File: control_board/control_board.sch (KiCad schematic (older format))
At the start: 38 parts, among them J1 Conn_01x08_Male, K1 G5Q-1A, Q1 Q_NPN_BEC, U1 MC78M05_TO252, U2 TSR_1-24120, U3 74LS02, U4 74LS02, U5 Conn_01x08_Male

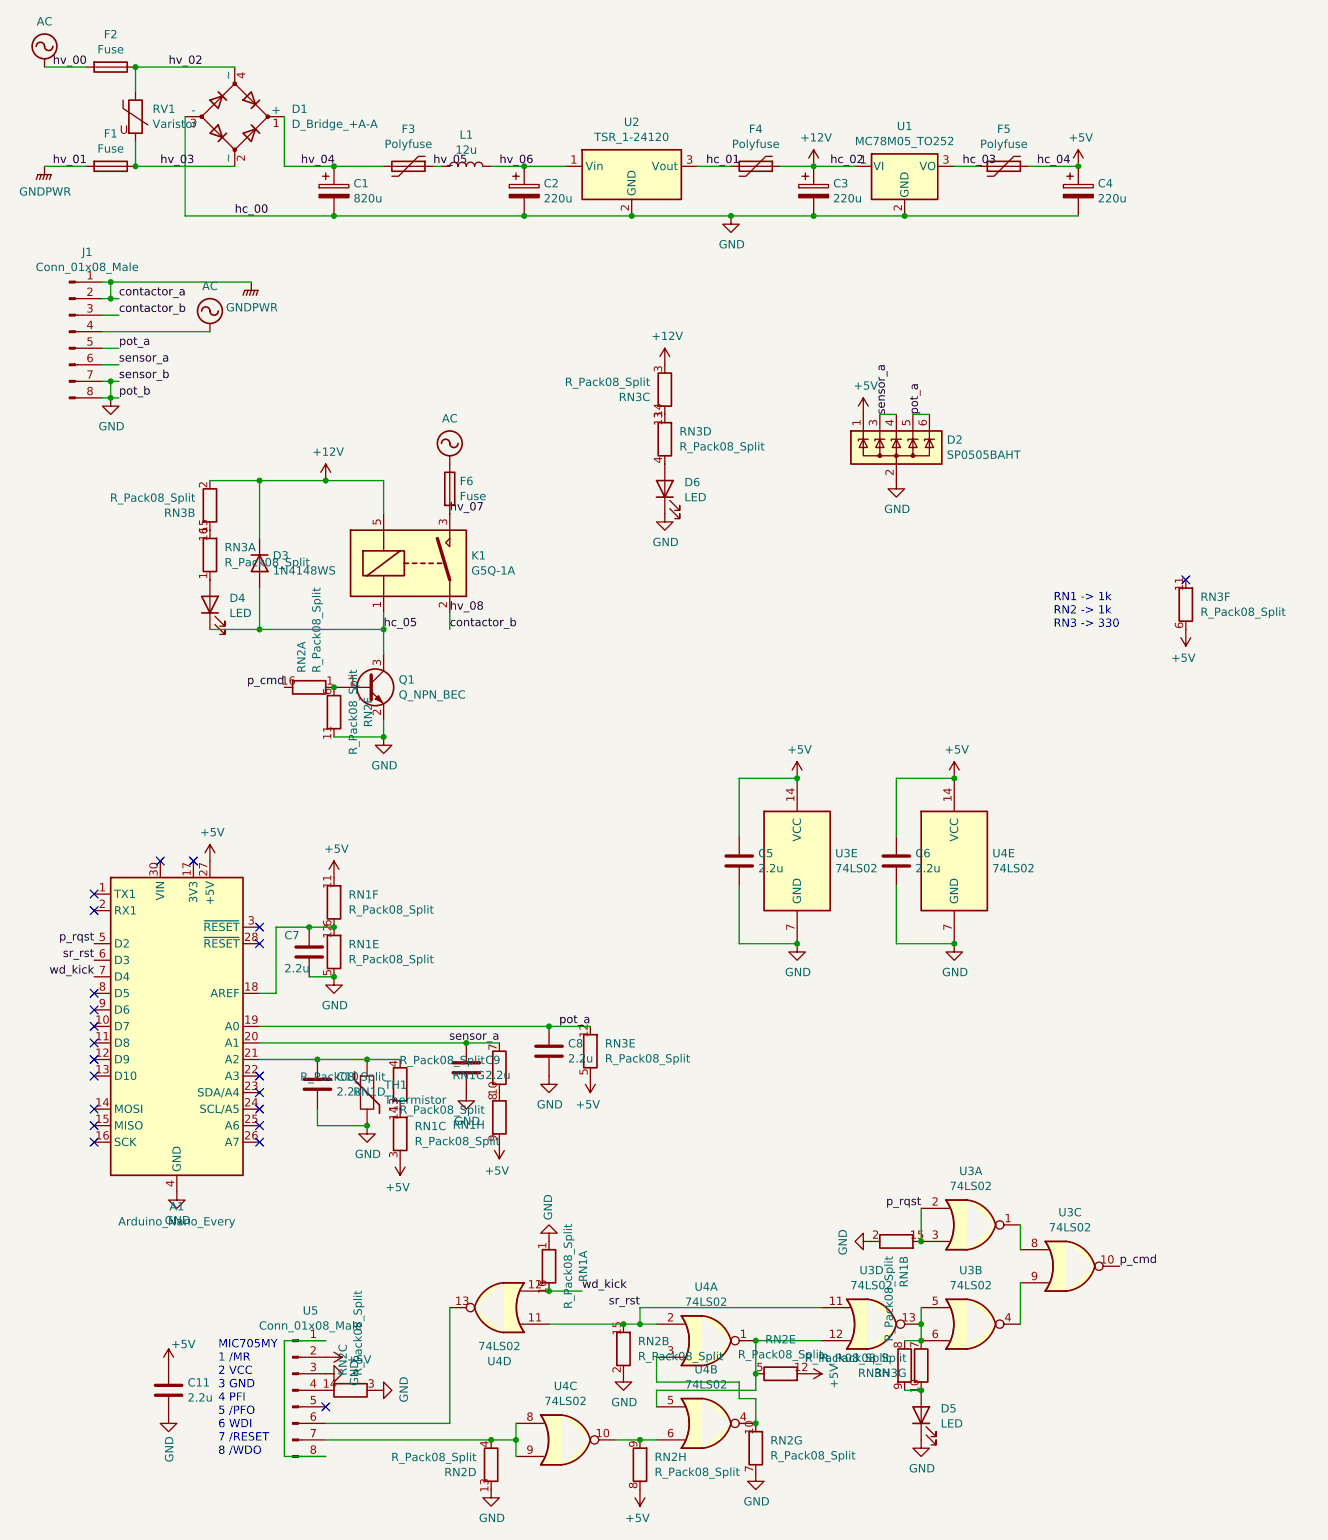
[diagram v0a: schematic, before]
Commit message: Revised PCB layout
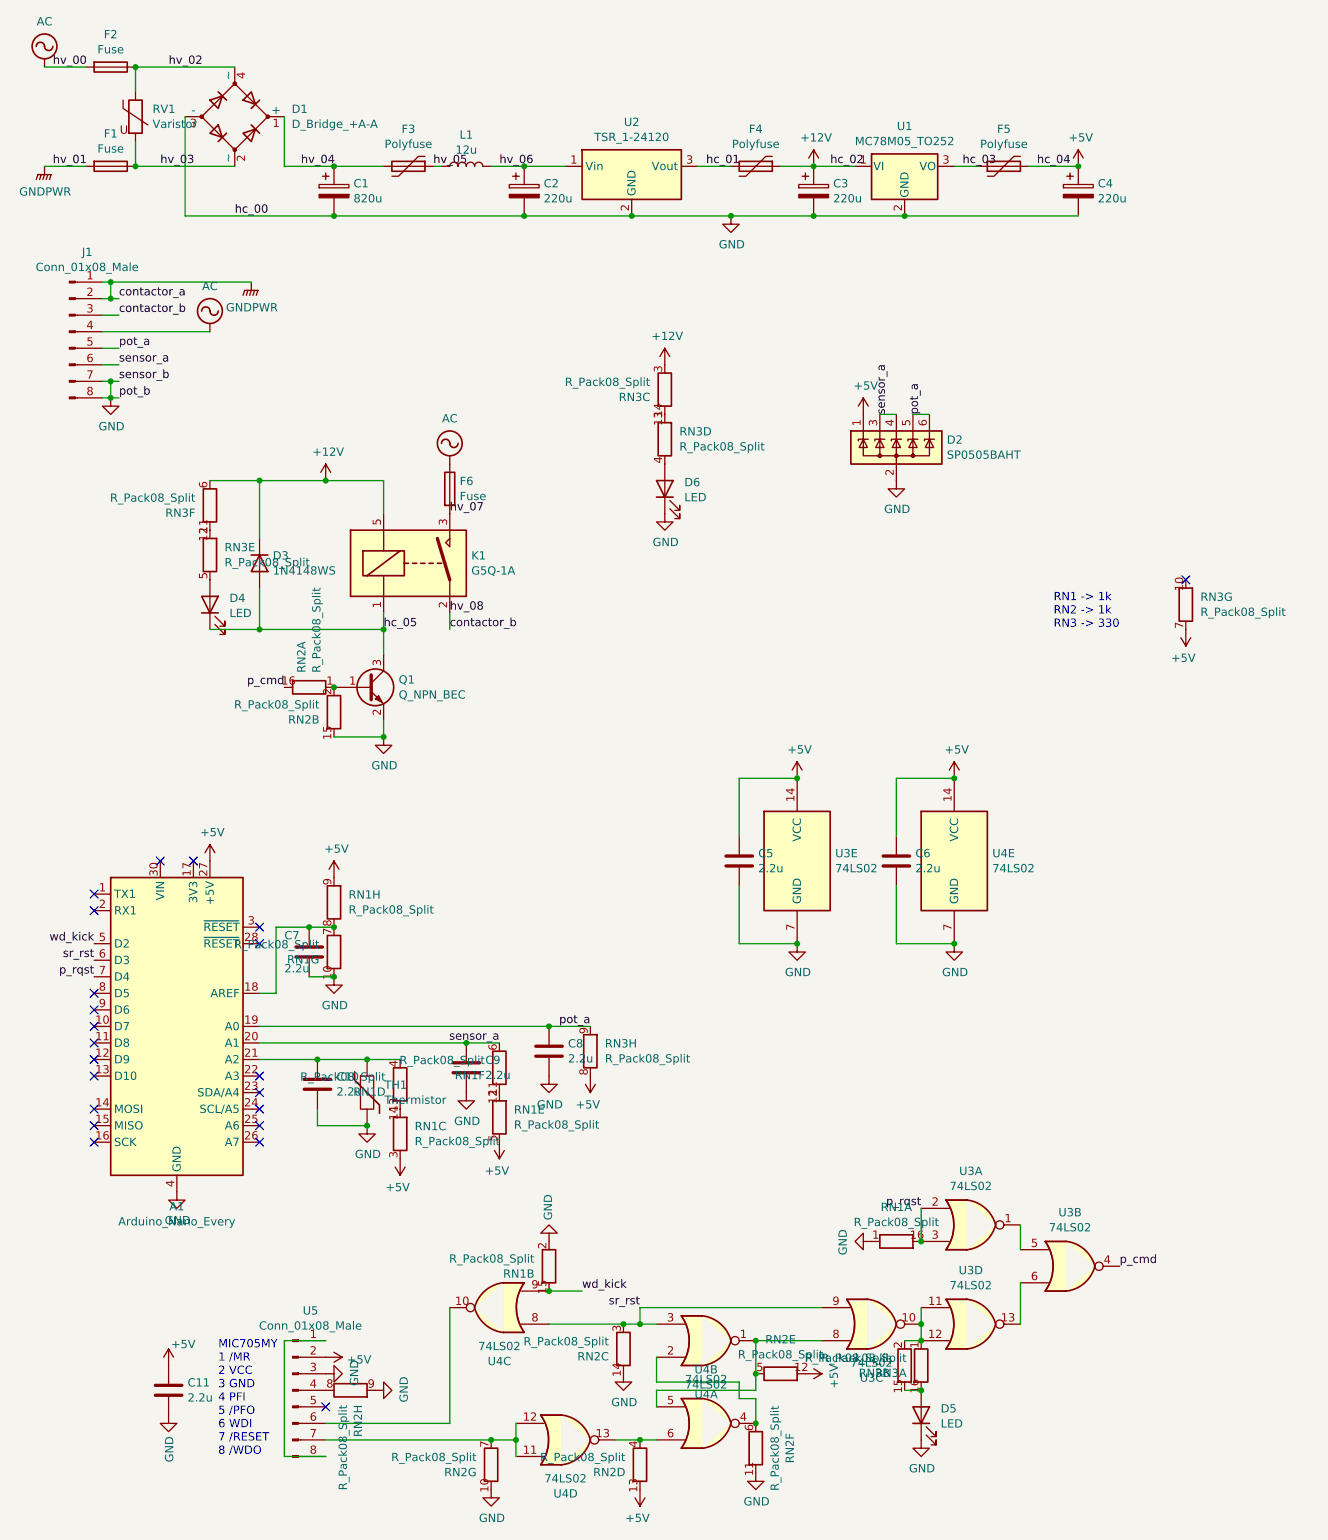
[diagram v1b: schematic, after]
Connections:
- net +12V: now also RN3.6 (R6.1); no longer RN3.2 (R2.1)
- net +5V: now also RN1.5 (R5.1), RN2.13 (R4.2), RN3.7 (R7.1), RN3.8 (R8.1); no longer RN1.11 (R6.2), RN2.8 (R8.1), RN3.5 (R5.1), RN3.6 (R6.1)
- net GND: now also RN1.10 (R7.2), RN2.10 (R7.2), RN2.14 (R3.2), RN2.15 (R2.2), RN2.9 (R8.2); no longer RN1.5 (R5.1), RN2.13 (R4.2), RN2.2 (R2.1), RN2.3 (R3.1), RN2.7 (R7.1)
- net p_cmd: now also U3.4; no longer U3.10
- net p_rqst: now also A1.7 (D4), RN1.16 (R1.2); no longer A1.5 (D2), RN1.15 (R2.2)
- net pot_a: now also RN3.9 (R8.2); no longer RN3.12 (R5.2)
- net sensor_a: now also RN1.6 (R6.1); no longer RN1.7 (R7.1)
- net sr_rst: now also RN2.3 (R3.1), U3.9, U4.3, U4.8; no longer RN2.15 (R2.2), U3.11, U4.11, U4.2
- net wd_kick: now also A1.5 (D2), RN1.15 (R2.2), U4.9; no longer A1.7 (D4), RN1.16 (R1.2), U4.12
- net at A1.18 (AREF), C7.1: now also RN1.7 (R7.1), RN1.8 (R8.1); no longer RN1.12 (R5.2), RN1.6 (R6.1)
- net at Q1.1 (B), RN2.1 (R1.1): now also RN2.2 (R2.1); no longer RN2.6 (R6.1)
- net at D4.2 (A): now also RN3.5 (R5.1); no longer RN3.1 (R1.1)
- net at U5.4 (Pin_4): now also RN2.8 (R8.1); no longer RN2.14 (R3.2)
- net at U5.6 (Pin_6): now also U4.10; no longer U4.13
- net at RN2.5 (R5.1), U4.1, U4.5: now also U3.8; no longer U3.12
- net at U3.1: now also U3.5; no longer U3.8
- net at RN3.15 (R2.2), RN3.16 (R1.2): now also D5.2 (A)
- net at RN3.11 (R6.2): now also RN3.12 (R5.2)
- new net: RN2.7 (R7.1), U4.11, U4.12, U5.7 (Pin_7)
- new net: RN2.6 (R6.1), U4.2, U4.4
- new net: RN2.4 (R4.1), U4.13, U4.6
- new net: RN3.1 (R1.1), RN3.2 (R2.1), U3.10, U3.11, U3.12
- new net: U3.13, U3.6
- new net: RN1.11 (R6.2), RN1.12 (R5.2)
- now unconnected: RN3.10 (R7.2)
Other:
- moved on the sheet: RN1A, RN1B, RN1E, RN1F, RN1G, RN1H, RN2B, RN2C, RN2D, RN2F, RN2G, RN2H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

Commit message: New mount hole spacing, new layout
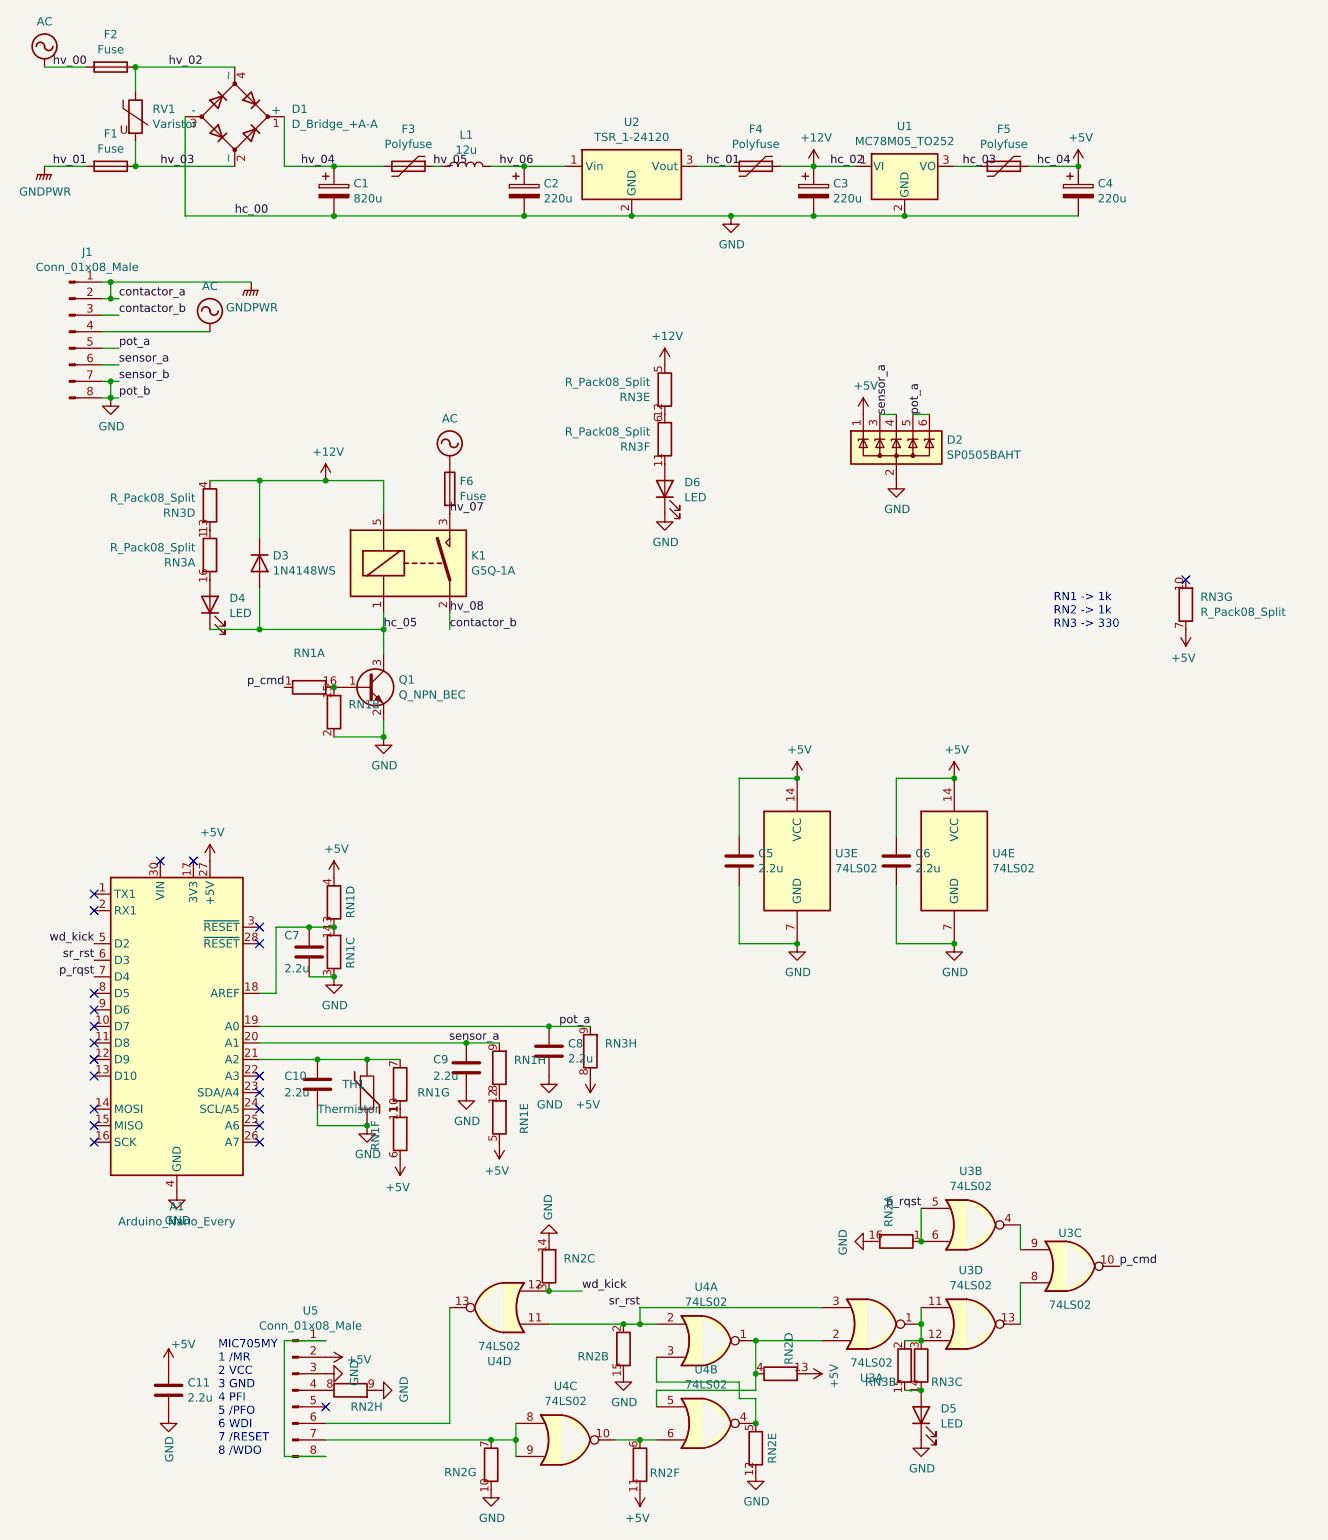
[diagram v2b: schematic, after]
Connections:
- net +12V: now also RN3.4 (R4.1), RN3.5 (R5.1); no longer RN3.3 (R3.1), RN3.6 (R6.1)
- net +5V: now also RN1.4 (R4.1), RN1.6 (R6.1), RN2.11 (R6.2); no longer RN1.3 (R3.1), RN1.9 (R8.2), RN2.12 (R5.2)
- net GND: now also RN1.3 (R3.1), RN2.12 (R5.2), RN2.16 (R1.2); no longer RN1.1 (R1.1), RN1.10 (R7.2), RN2.11 (R6.2)
- net p_cmd: now also RN1.1 (R1.1), U3.10; no longer RN2.16 (R1.2), U3.4
- net p_rqst: now also RN2.1 (R1.1), U3.5, U3.6; no longer RN1.16 (R1.2), U3.2, U3.3
- net sensor_a: now also RN1.9 (R8.2); no longer RN1.6 (R6.1)
- net sr_rst: now also RN2.2 (R2.1), U3.3, U4.11, U4.2; no longer RN2.3 (R3.1), U3.9, U4.3, U4.8
- net wd_kick: now also RN2.3 (R3.1), U4.12; no longer RN1.15 (R2.2), U4.9
- net at A1.18 (AREF), C7.1: now also RN1.13 (R4.2), RN1.14 (R3.2); no longer RN1.7 (R7.1), RN1.8 (R8.1)
- net at A1.21 (A2), C10.1, TH1.1: now also RN1.7 (R7.1); no longer RN1.4 (R4.1)
- net at D4.2 (A): now also RN3.16 (R1.2); no longer RN3.5 (R5.1)
- net at U5.6 (Pin_6): now also U4.13; no longer U4.10
- net at RN2.7 (R7.1), U5.7 (Pin_7): now also U4.8, U4.9; no longer U4.11, U4.12
- net at U4.1, U4.5: now also RN2.4 (R4.1), U3.2; no longer RN2.5 (R5.1), U3.8
- net at RN3.2 (R2.1), U3.11, U3.12: now also RN3.3 (R3.1), U3.1; no longer RN3.1 (R1.1), U3.10
- net at U3.13: now also U3.8; no longer U3.6
- net at D5.2 (A), RN3.15 (R2.2): now also RN3.14 (R3.2); no longer RN3.16 (R1.2)
- net at RN1.12 (R5.2): now also RN1.8 (R8.1); no longer RN1.11 (R6.2)
- net at D6.2 (A): now also RN3.11 (R6.2); no longer RN3.4 (R4.1)
- net at RN3.13 (R4.2): now also RN3.1 (R1.1); no longer RN3.14 (R3.2)
- net at RN3.12 (R5.2): now also RN3.6 (R6.1); no longer RN3.11 (R6.2)
- new net: Q1.1 (B), RN1.15 (R2.2), RN1.16 (R1.2)
- new net: RN2.5 (R5.1), U4.3, U4.4
- new net: RN2.6 (R6.1), U4.10, U4.6
- new net: U3.4, U3.9
- new net: RN1.10 (R7.2), RN1.11 (R6.2)
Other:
- moved on the sheet: RN1A, RN1B, RN1C, RN1D, RN1F, RN1G, RN1H, RN2A, RN2B, RN2C, RN2D, RN2E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
